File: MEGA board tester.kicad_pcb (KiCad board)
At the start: 2 copper layers, 119.4 x 53.3 mm, 93 parts, among them J1 Arduino_Mega_Header

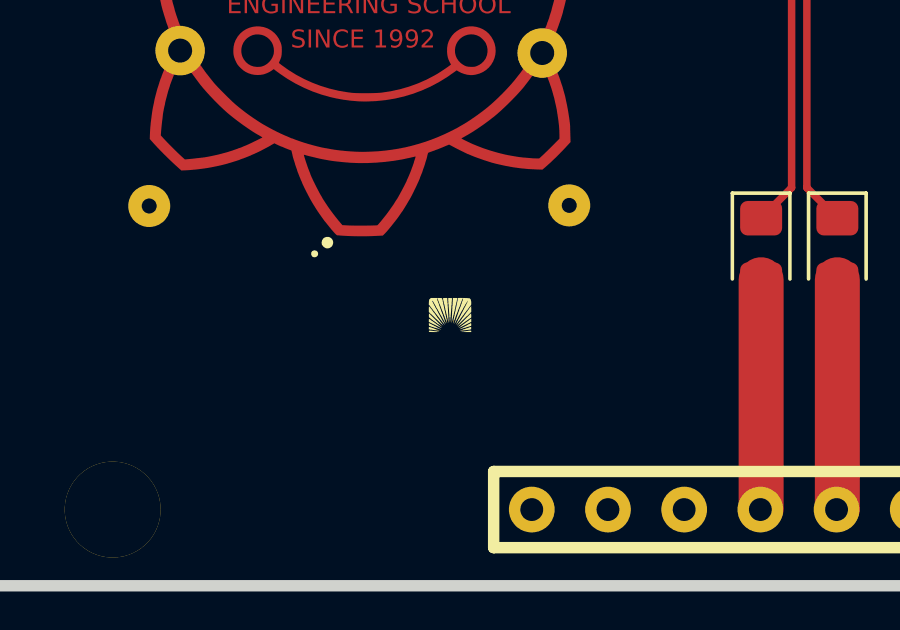
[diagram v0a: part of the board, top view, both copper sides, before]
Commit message: PCB, schematic, and code update
PCB update:
- removed the rising sung logo as it was not fab-friendly (was removed by the fab-house from the fab'd PCB)
- updated version to 1.1
- added version and date on User.Drawing layer
- there is a known problem where the data transmission will not happen on arduino if the test board is plugged in, due to pins 0 and 1 (D0 & D1) being used by the board tester. Only (untested) fix for now is to disconnect those two paths from ground by either not populating the pins, or cutting the traces at any point before RN5).

Schematic:
- cleanup. added '150R x4' as value to the resistor networks in place of 'Rpack04'

Code:
- cleanup
- added bit of code to work with Arduino Uno properly, you just need to change `int type = 0` according to which board is being programmed. this needs/will be automated in a future revision.
- added code version and code date at top of code, starting at V1.
- incremented code version at top of code, to V1.1
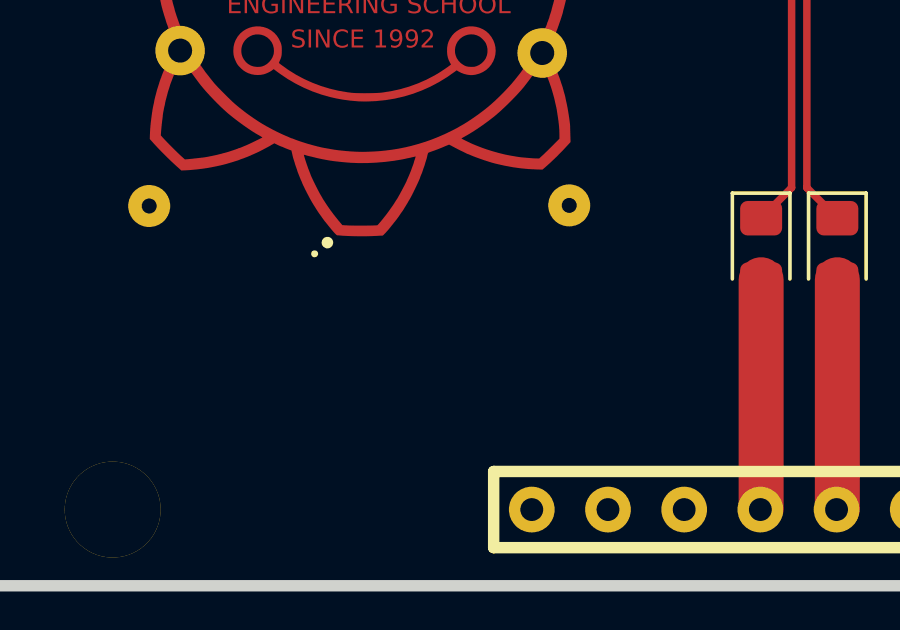
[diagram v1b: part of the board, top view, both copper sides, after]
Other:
- board text added: "Version 1.1"
- board text added: "v1.1, 3/25/2023"
- board text removed: "Version 1"

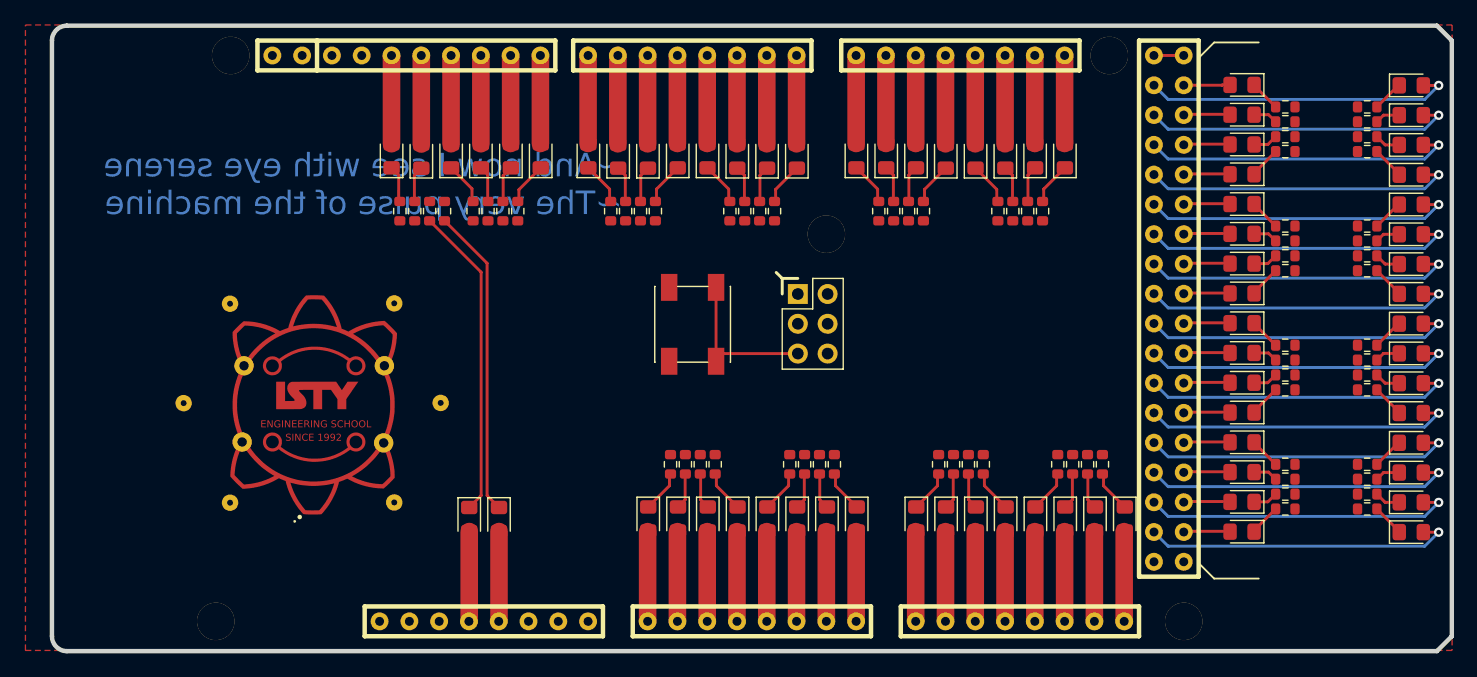
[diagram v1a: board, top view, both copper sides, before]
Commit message: PCB updated to version 2 added  ∅D20, ∅D21, ∅D38, to ensure compatibility with Arduino Zero boards. (D38 is called ANT on the board, unnamed on mega and unoR3) moved the ISTY logo and credits to make place for new components added a QR code linking to the repo on the back updated version on board tweaked placement of a few component names. OCD.
have yet to decide on what to do with D0 and D1 so they don't interfere with program upload. leave them? remove them and put in test loops for probing? tbd.
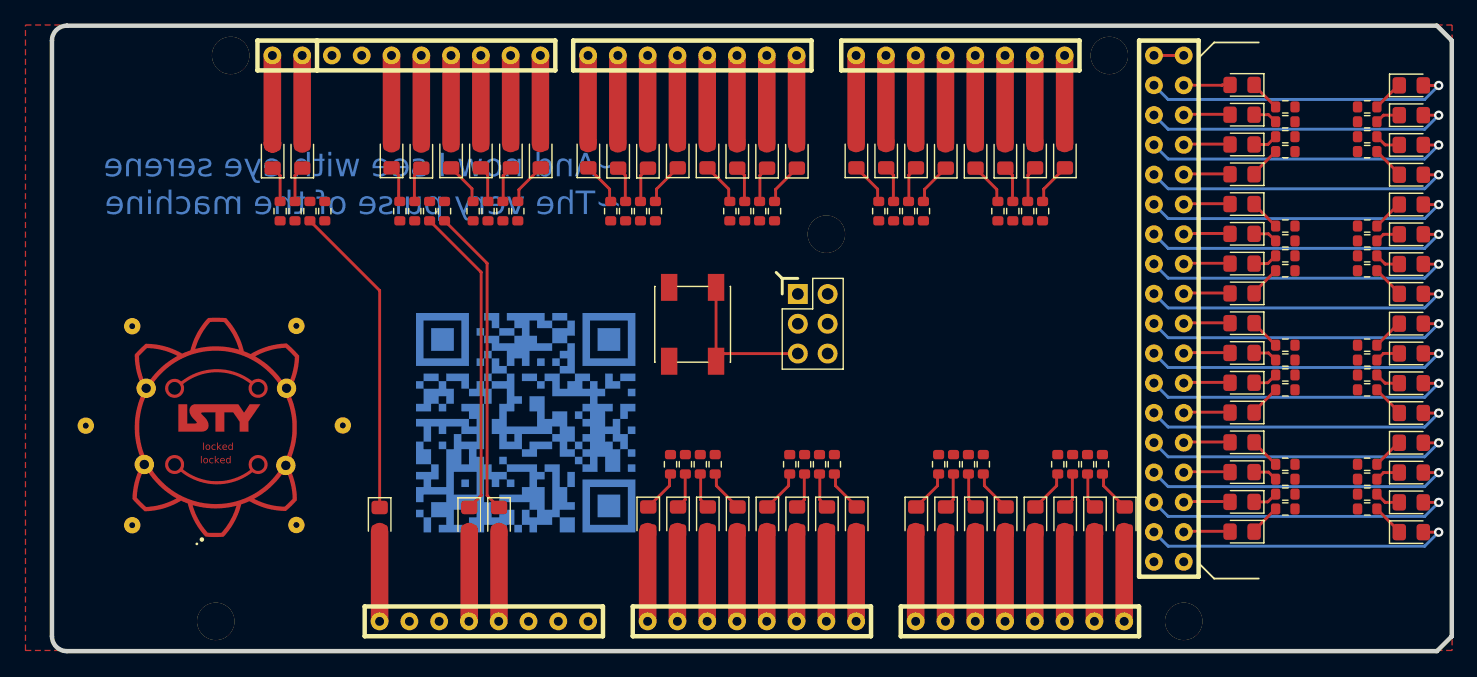
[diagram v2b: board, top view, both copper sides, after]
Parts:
- added G*** (x2): LOGO, LOGO, B.Cu at (172.5, 84.7)
- added RN1: 150R x4, Components:R_Array_convex_EXB-S8Vxxxx, F.Cu at (153.4, 66.7)
- added ∅D20: LED, Diode_SMD:D_0805_2012Metric_Pad1.15x1.40mm_HandSolder, F.Cu at (153.4, 62.0)
- added ∅D21: LED, Diode_SMD:D_0805_2012Metric_Pad1.15x1.40mm_HandSolder, F.Cu at (150.9, 62.0)
- added ∅D38: LED, Diode_SMD:D_0805_2012Metric_Pad1.15x1.40mm_HandSolder, F.Cu at (160.0, 93.0)
- RN10: renamed from RN9; value R_Pack04 -> 150R x4; footprint components:R_Array_convex_EXB-S8Vxxxx -> Components:R_Array_convex_EXB-S8Vxxxx
- RN11: renamed from RN10; value R_Pack04 -> 150R x4; footprint components:R_Array_convex_EXB-S8Vxxxx -> Components:R_Array_convex_EXB-S8Vxxxx
- RN12, RN14, RN16, RN18: value R_Pack04 -> 150R x4; footprint components:R_Array_convex_EXB-S8Vxxxx -> Components:R_Array_convex_EXB-S8Vxxxx
- RN13: renamed from RN11; value R_Pack04 -> 150R x4; footprint components:R_Array_convex_EXB-S8Vxxxx -> Components:R_Array_convex_EXB-S8Vxxxx
- RN15: renamed from RN13; value R_Pack04 -> 150R x4; footprint components:R_Array_convex_EXB-S8Vxxxx -> Components:R_Array_convex_EXB-S8Vxxxx
- RN17: renamed from RN15; value R_Pack04 -> 150R x4; footprint components:R_Array_convex_EXB-S8Vxxxx -> Components:R_Array_convex_EXB-S8Vxxxx
- RN19: renamed from RN17; value R_Pack04 -> 150R x4; footprint components:R_Array_convex_EXB-S8Vxxxx -> Components:R_Array_convex_EXB-S8Vxxxx
- RN2: renamed from RN1; value R_Pack04 -> 150R x4; footprint components:R_Array_convex_EXB-S8Vxxxx -> Components:R_Array_convex_EXB-S8Vxxxx
- RN3: renamed from RN2; value R_Pack04 -> 150R x4; footprint components:R_Array_convex_EXB-S8Vxxxx -> Components:R_Array_convex_EXB-S8Vxxxx
- RN4: renamed from RN3; value R_Pack04 -> 150R x4; footprint components:R_Array_convex_EXB-S8Vxxxx -> Components:R_Array_convex_EXB-S8Vxxxx
- RN5: renamed from RN4; value R_Pack04 -> 150R x4; footprint components:R_Array_convex_EXB-S8Vxxxx -> Components:R_Array_convex_EXB-S8Vxxxx
- RN6: renamed from RN5; value R_Pack04 -> 150R x4; footprint components:R_Array_convex_EXB-S8Vxxxx -> Components:R_Array_convex_EXB-S8Vxxxx
- RN7: renamed from RN6; value R_Pack04 -> 150R x4; footprint components:R_Array_convex_EXB-S8Vxxxx -> Components:R_Array_convex_EXB-S8Vxxxx
- RN8: renamed from RN7; value R_Pack04 -> 150R x4; footprint components:R_Array_convex_EXB-S8Vxxxx -> Components:R_Array_convex_EXB-S8Vxxxx
- RN9: renamed from RN8; value R_Pack04 -> 150R x4; footprint components:R_Array_convex_EXB-S8Vxxxx -> Components:R_Array_convex_EXB-S8Vxxxx
- renumbered REF** to Logo1
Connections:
- J1 pad 1: unconnected-(J1-Pad1) -> Net-(J1-Pad1)
- J1 pad 85: unconnected-(J1-Pad85) -> Net-(J1-Pad85)
- J1 pad 86: unconnected-(J1-Pad86) -> Net-(J1-Pad86)
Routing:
- net Net-(RN1-Pad7): track 0.00 -> 26.9 mm
- net Net-(J1-Pad1): track 0.00 -> 7.66 mm
- net Net-(J1-Pad86): track 0.00 -> 7.56 mm
- net Net-(J1-Pad85): track 0.00 -> 7.55 mm
- net Net-(RN1-Pad4): track 0.00 -> 3.11 mm
- net Net-(RN1-Pad3): track 0.00 -> 3.11 mm
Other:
- board text added: "Version 2"
- board text added: "v2, 28/03/2023"
- board text removed: "Version 1.1"
- board text removed: "v1.1, 3/25/2023"
